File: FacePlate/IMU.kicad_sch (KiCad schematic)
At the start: 8 parts, among them U3 ICM-20689

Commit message: Ordered faceplate
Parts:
- C? (x2): LCSC (none) -> C96446
- R29, R30: value 10k -> 13k; LCSC C25744 -> C22797
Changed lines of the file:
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@@
+      (effects (font (size 1.27 1.27)) hide)
+    )
+    (property "LCSC" "C96446" (at 143.51 69.85 0)
       (effects (font (size 1.27 1.27)) hide)
     )
@@
       (effects (font (size 1.27 1.27)) (justify left))
     )
-    (property "Value" "10k" (at 60.96 76.2 0)
+    (property "Value" "13k" (at 60.96 76.2 0)
       (effects (font (size 1.27 1.27)) (justify left))
     )
@@
       (effects (font (size 1.27 1.27)) hide)
     )
-    (property "LCSC" "C25744" (at 58.42 74.93 0)
+    (property "LCSC" "C22797" (at 58.42 74.93 0)
       (effects (font (size 1.27 1.27)) hide)
     )
@@
       (effects (font (size 1.27 1.27)) (justify left))
     )
-    (property "Value" "10k" (at 41.91 66.04 0)
+    (property "Value" "13k" (at 41.91 66.04 0)
       (effects (font (size 1.27 1.27)) (justify left))
     )
@@
       (effects (font (size 1.27 1.27)) hide)
     )
-    (property "LCSC" "C25744" (at 39.37 64.77 0)
+    (property "LCSC" "C22797" (at 39.37 64.77 0)
       (effects (font (size 1.27 1.27)) hide)
     )
@@
       (effects (font (size 1.27 1.27)) hide)
     )
+    (property "LCSC" "C96446" (at 119.38 69.85 0)
+      (effects (font (size 1.27 1.27)) hide)
+    )

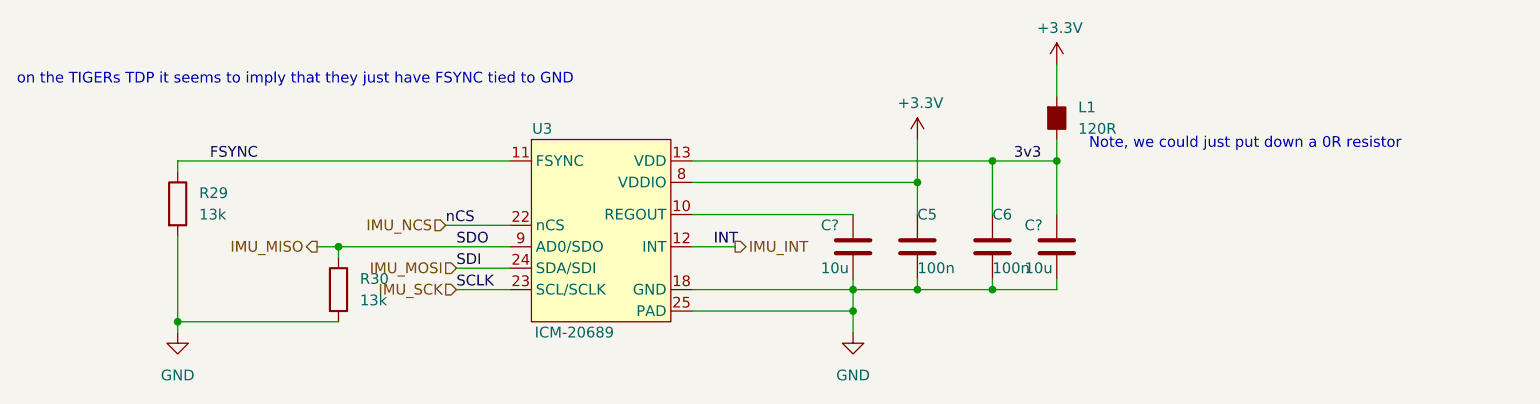
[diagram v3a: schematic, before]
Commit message: changed transceiver for faceplate
+ removed caps on chicker can
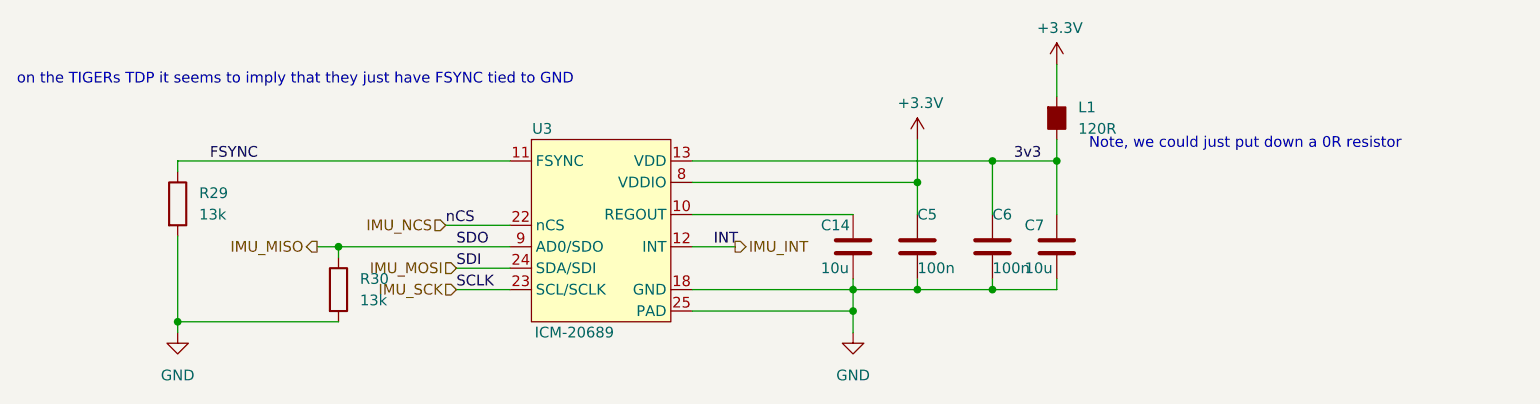
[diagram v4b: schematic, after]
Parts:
- gave numbers to parts that had none: 2

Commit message: faceplate global files working
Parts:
- C14, C7: footprint bots:C_0603_1608Metric -> bots:C_0805_2012Metric; symbol Device:C -> bots:C_10u; JLC (none) -> 0805; JLC Extended (none) -> no; LCSC C96446 -> C440198; MPN (none) -> GRM21BR61H106KE43L; Manufacturer (none) -> Murata; Price (none) -> 0.0645
- R29, R30: symbol bots:10k -> bots:R_13k; JLC (none) -> 0603; JLC Extended (none) -> no; MPN (none) -> 0603WAF1302T5E; Manufacturer (none) -> UNI-ROYAL(Uniroyal Elec); Price (none) -> 0.0008
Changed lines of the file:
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@@
 	)
 	(symbol
-		(lib_id "Device:C")
+		(lib_id "bots:C_10u")
 		(at 143.51 69.85 0)
 		(unit 1)
@@
 			)
 		)
-		(property "Footprint" "bots:C_0603_1608Metric"
+		(property "Footprint" "bots:C_0805_2012Metric"
 			(at 144.4752 73.66 0)
 			(effects
@@
 			)
 		)
-		(property "Description" ""
+		(property "Description" "Unpolarized capacitor"
 			(at 143.51 69.85 0)
 			(effects
@@
 					(size 1.27 1.27)
 				)
-			)
-		)
-		(property "LCSC" "C96446"
+				(hide yes)
+			)
+		)
+		(property "LCSC" "C440198"
+			(at 143.51 69.85 0)
+			(effects
+				(font
+					(size 1.27 1.27)
+				)
+				(hide yes)
+			)
+		)
+		(property "MPN" "GRM21BR61H106KE43L"
+			(at 143.51 69.85 0)
+			(effects
+				(font
+					(size 1.27 1.27)
+				)
+				(hide yes)
+			)
+		)
+		(property "Manufacturer" "Murata"
+			(at 143.51 69.85 0)
+			(effects
+				(font
+					(size 1.27 1.27)
+				)
+				(hide yes)
+			)
+		)
+		(property "Price" "0.0645"
+			(at 143.51 69.85 0)
+			(effects
+				(font
+					(size 1.27 1.27)
+				)
+				(hide yes)
+			)
+		)
+		(property "JLC" "0805"
+			(at 143.51 69.85 0)
+			(effects
+				(font
+					(size 1.27 1.27)
+				)
+				(hide yes)
+			)
+		)
+		(property "JLC Extended" "no"
 			(at 143.51 69.85 0)
 			(effects
@@
 	)
 	(symbol
-		(lib_id "bots:10k")
+		(lib_id "bots:R_13k")
 		(at 58.42 74.93 0)
 		(unit 1)
@@
 		(fields_autoplaced yes)
 		(property "Reference" "R30"
-			(at 60.96 73.66 0)
+			(at 60.96 73.6599 0)
 			(effects
 				(font
@@
 		)
 		(property "Value" "13k"
-			(at 60.96 76.2 0)
+			(at 60.96 76.1999 0)
 			(effects
 				(font
@@
 			)
 		)
-		(property "Description" ""
+		(property "Description" "Resistor"
 			(at 58.42 74.93 0)
 			(effects
@@
 					(size 1.27 1.27)
 				)
+				(hide yes)
 			)
 		)
 		(property "LCSC" "C22797"
+			(at 58.42 74.93 0)
+			(effects
+				(font
+					(size 1.27 1.27)
+				)
+				(hide yes)
+			)
+		)
+		(property "MPN" "0603WAF1302T5E"
+			(at 58.42 74.93 0)
+			(effects
+				(font
+					(size 1.27 1.27)
+				)
+				(hide yes)
+			)
+		)
+		(property "Manufacturer" "UNI-ROYAL(Uniroyal Elec)"
+			(at 58.42 74.93 0)
+			(effects
+				(font
+					(size 1.27 1.27)
+				)
+				(hide yes)
+			)
+		)
+		(property "Price" "0.0008"
+			(at 58.42 74.93 0)
+			(effects
+				(font
+					(size 1.27 1.27)
+				)
+				(hide yes)
+			)
+		)
+		(property "JLC" "0603"
+			(at 58.42 74.93 0)
+			(effects
+				(font
+					(size 1.27 1.27)
+				)
+				(hide yes)
+			)
+		)
+		(property "JLC Extended" "no"
 			(at 58.42 74.93 0)
 			(effects
@@
 	)
 	(symbol
-		(lib_id "bots:10k")
+		(lib_id "bots:R_13k")
 		(at 39.37 64.77 0)
 		(unit 1)
@@
 		(fields_autoplaced yes)
 		(property "Reference" "R29"
-			(at 41.91 63.5 0)
+			(at 41.91 63.4999 0)
 			(effects
 				(font
@@
 		)
 		(property "Value" "13k"
-			(at 41.91 66.04 0)
+			(at 41.91 66.0399 0)
 			(effects
 				(font
@@
 			)
 		)
-		(property "Description" ""
+		(property "Description" "Resistor"
 			(at 39.37 64.77 0)
 			(effects
@@
 					(size 1.27 1.27)
 				)
+				(hide yes)
 			)
 		)
 		(property "LCSC" "C22797"
+			(at 39.37 64.77 0)
+			(effects
+				(font
+					(size 1.27 1.27)
+				)
+				(hide yes)
+			)
+		)
+		(property "MPN" "0603WAF1302T5E"
+			(at 39.37 64.77 0)
+			(effects
+				(font
+					(size 1.27 1.27)
+				)
+				(hide yes)
+			)
+		)
+		(property "Manufacturer" "UNI-ROYAL(Uniroyal Elec)"
+			(at 39.37 64.77 0)
+			(effects
+				(font
+					(size 1.27 1.27)
+				)
+				(hide yes)
+			)
+		)
+		(property "Price" "0.0008"
+			(at 39.37 64.77 0)
+			(effects
+				(font
+					(size 1.27 1.27)
+				)
+				(hide yes)
+			)
+		)
+		(property "JLC" "0603"
+			(at 39.37 64.77 0)
+			(effects
+				(font
+					(size 1.27 1.27)
+				)
+				(hide yes)
+			)
+		)
+		(property "JLC Extended" "no"
 			(at 39.37 64.77 0)
 			(effects
@@
 	)
 	(symbol
-		(lib_id "Device:C")
+		(lib_id "bots:C_10u")
 		(at 119.38 69.85 0)
 		(unit 1)
@@
 			)
 		)
-		(property "Footprint" "bots:C_0603_1608Metric"
+		(property "Footprint" "bots:C_0805_2012Metric"
 			(at 120.3452 73.66 0)
 			(effects
@@
 			)
 		)
-		(property "Description" ""
+		(property "Description" "Unpolarized capacitor"
 			(at 119.38 69.85 0)
 			(effects
@@
 					(size 1.27 1.27)
 				)
-			)
-		)
-		(property "LCSC" "C96446"
+				(hide yes)
+			)
+		)
+		(property "LCSC" "C440198"
 			(at 119.38 69.85 0)
 			(effects
+				(font
+					(size 1.27 1.27)
+				)
+				(hide yes)
+			)
+		)
+		(property "MPN" "GRM21BR61H106KE43L"
+			(at 119.38 69.85 0)
+			(effects
+				(font
+					(size 1.27 1.27)
+				)
+				(hide yes)
+			)
+		)
+		(property "Manufacturer" "Murata"
+			(at 119.38 69.85 0)
+			(effects
+				(font
+					(size 1.27 1.27)
+				)
+				(hide yes)
+			)
+		)
+		(property "Price" "0.0645"
+			(at 119.38 69.85 0)
+			(effects
+				(font
+					(size 1.27 1.27)
+				)
+				(hide yes)
+			)
+		)
+		(property "JLC" "0805"
+			(at 119.38 69.85 0)
+			(effects
+				(font
+					(size 1.27 1.27)
+				)
+				(hide yes)
+			)
+		)
+		(property "JLC Extended" "no"
+			(at 119.38 69.85 0)
+			(effects

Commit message: added a title block
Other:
- company: (none) -> The Bots
- title: (none) -> Faceplate
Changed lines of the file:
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@@
 	(generator "eeschema")
 	(generator_version "9.0")
-	(paper "A5")
+	(paper "A4")
+	(title_block
+		(title "Faceplate")
+		(date "2024-02-04")
+		(rev "V1.0")
+		(company "The Bots")
+	)
 	(text "Note, we could just put down a 0R resistor"
 		(exclude_from_sim no)
